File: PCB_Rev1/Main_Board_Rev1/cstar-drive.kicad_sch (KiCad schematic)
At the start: 0 parts

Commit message: LDO component files imported
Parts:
- added C15: C_Polarized, symbol Device:C_Polarized
- added CR1, CR2: SP4022-01FTG-C, CSTAR-MainBoard-Footprints:ZDO_SP4022_LTF, symbol SP4022_01FTG_C:SP4022-01FTG-C
- added D2, D3, D4, D5, D6, D7, D8, D9: D, symbol Device:D
- added J10, J9: B4B-PH-K-S, CSTAR-MainBoard-Footprints:B4B_PH_K_S, symbol B4B_PH_K_S:B4B-PH-K-S
- added U2: L298N, Package_TO_SOT_THT:TO-220-15_P2.54x2.54mm_StaggerOdd_Lead4.58mm_Vertical, symbol Driver_Motor:L298N
- added X1, X2: B2P-VH, CSTAR-MainBoard-Footprints:B2P-VH, symbol B2P-VH:B2P-VH
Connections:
- new net +3V3: J10.1, J9.1
- new net +5V: C15.1, D2.1 (K), D4.1 (K), D6.1 (K), D8.1 (K), U2.4 (Vs), U2.9 (Vss)
- new net Ch.A_MOTOR_1: J9.3
- new net Ch.A_MOTOR_2: J10.3
- new net Ch.B_MOTOR_1: J9.4
- new net Ch.B_MOTOR_2: J10.4
- new net EN_MOTOR_1: U2.6 (EnA)
- new net EN_MOTOR_2: U2.11 (EnB)
- new net GND: C15.2, D3.2 (A), D5.2 (A), D7.2 (A), D9.2 (A), J10.2, J9.2, U2.1 (SENSE_A), U2.15 (SENSE_B), U2.8 (GND)
- new net IN1_MOTOR_1: U2.5 (IN1)
- new net IN1_MOTOR_2: U2.10 (IN3)
- new net IN2_MOTOR_1: U2.7 (IN2)
- new net IN2_MOTOR_2: U2.12 (IN4)
- new net OUT1_MOTOR_1: CR1.2, D2.2 (A), D3.1 (K), U2.2 (OUT1), X1.1
- new net OUT1_MOTOR_2: CR2.2, D6.2 (A), D7.1 (K), U2.13 (OUT3), X2.1
- new net OUT2_MOTOR_1: CR1.1, D4.2 (A), D5.1 (K), U2.3 (OUT2), X1.2
- new net OUT2_MOTOR_2: CR2.1, D8.2 (A), D9.1 (K), U2.14 (OUT4), X2.2
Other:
- note added: "ENCODER 1 CONNECTION"
- note added: "ENCODER 2 CONNECTION"
- note added: "MOTOR 1 CONNECTION"
- note added: "MOTOR 2 CONNECTION"
- note added: "MOTOR DRIVE TRAIN SCHEMATIC"
- note added: "MOTOR DRIVER"

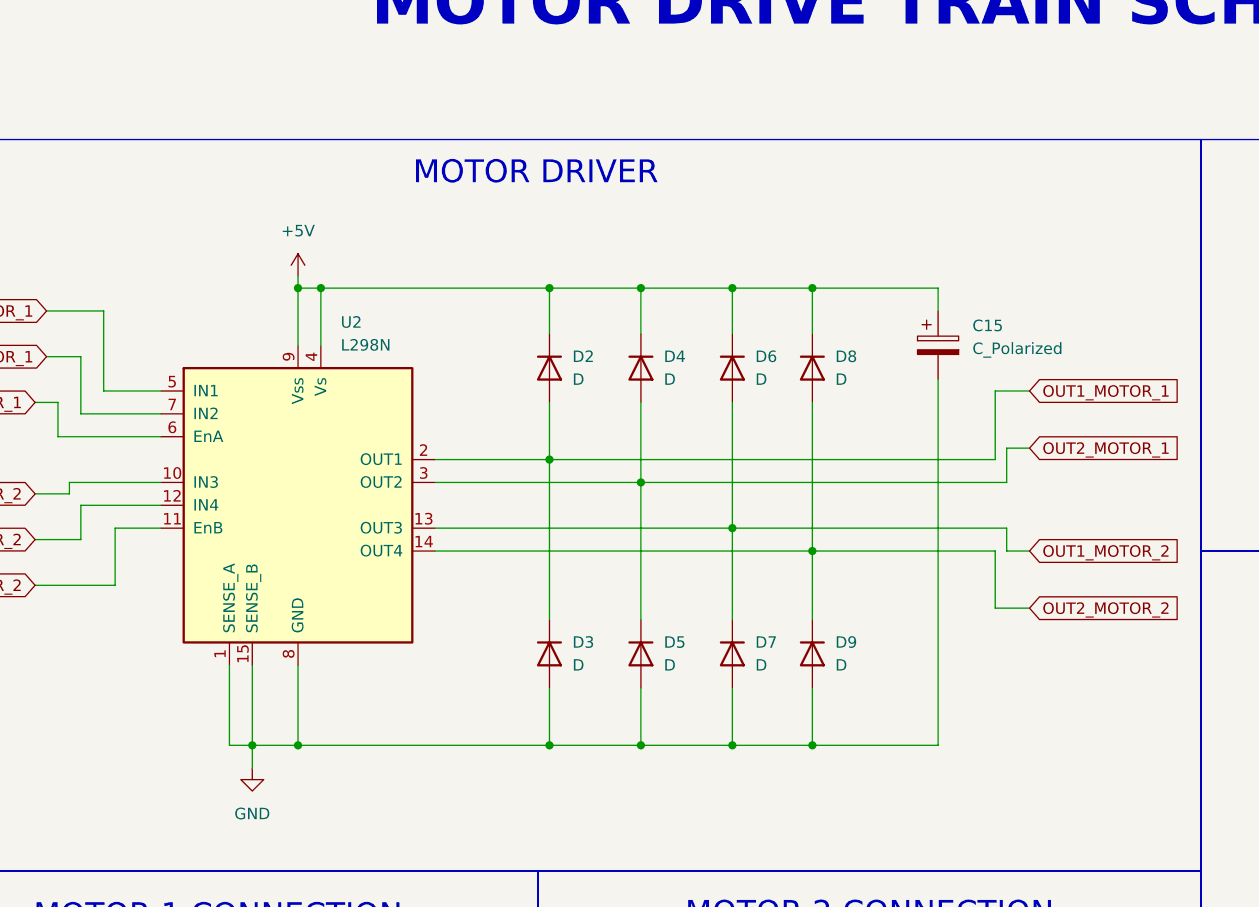
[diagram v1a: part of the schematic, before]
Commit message: Driver Schematic Update
Vss / Vs and decoupling capacitor updates
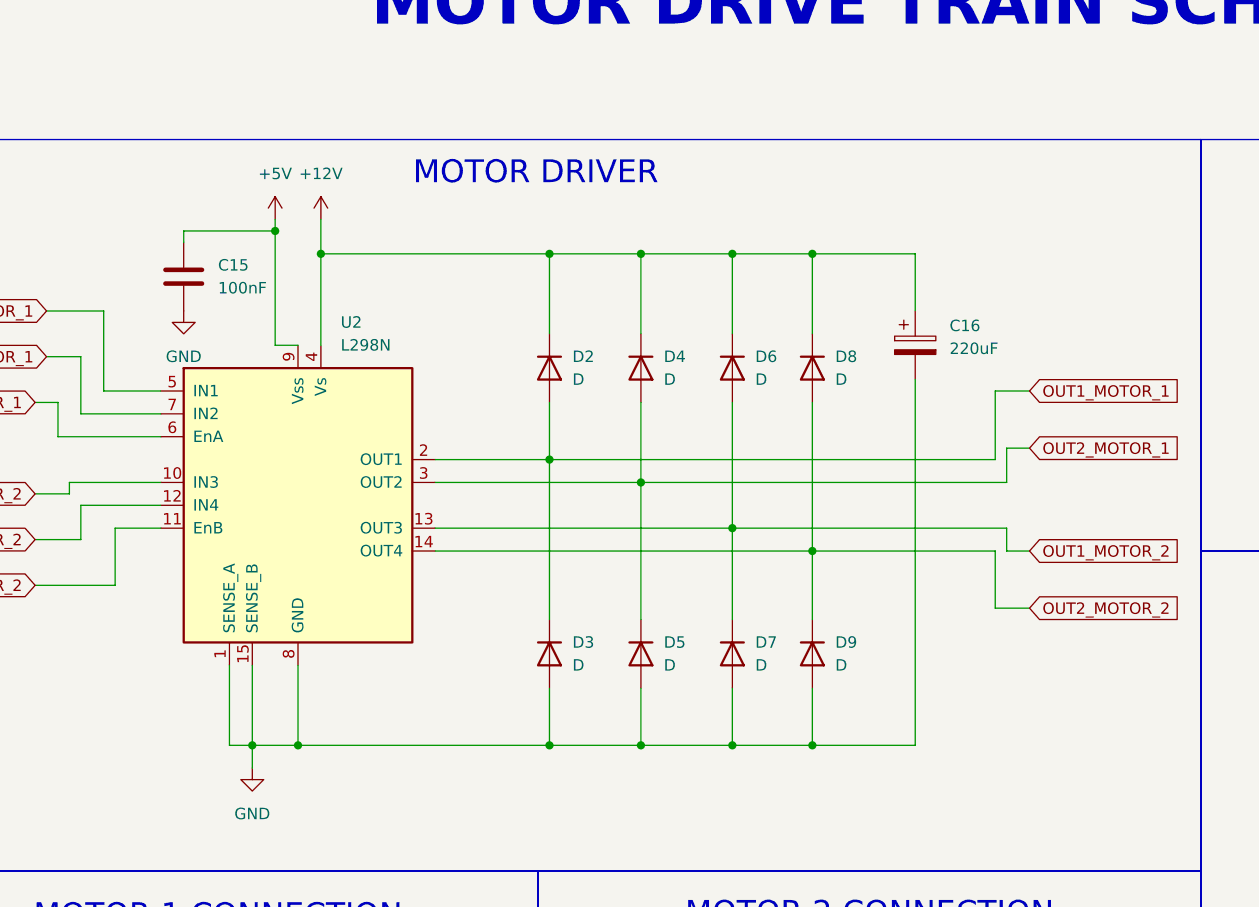
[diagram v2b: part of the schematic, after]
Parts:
- removed C15: C_Polarized, symbol Device:C_Polarized
- added C15: 100nF, symbol Device:C
- added C16: 220uF, symbol Device:C_Polarized
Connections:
- net +5V: now also C15.1; no longer D2.1 (K), D4.1 (K), D6.1 (K), D8.1 (K), U2.4 (Vs)
- net GND: now also C15.2, C16.2
- new net +12V: C16.1, D2.1 (K), D4.1 (K), D6.1 (K), D8.1 (K), U2.4 (Vs)

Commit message: Passives footprints changed
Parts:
- C15, C16: footprint (none) -> Capacitor_SMD:C_0805_2012Metric
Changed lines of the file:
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@@
 			)
 		)
-		(property "Footprint" ""
+		(property "Footprint" "Capacitor_SMD:C_0805_2012Metric"
 			(at 60.6552 62.23 0)
 			(effects
@@
 			)
 		)
-		(property "Footprint" ""
+		(property "Footprint" "Capacitor_SMD:C_0805_2012Metric"
 			(at 141.9352 69.85 0)
 			(effects

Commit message: Added new footprints
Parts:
- J10, J9: footprint CSTAR-MainBoard-Footprints:B4B_PH_K_S -> (none)
- X1, X2: footprint CSTAR-MainBoard-Footprints:B2P-VH -> (none)
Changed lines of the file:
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@@
 			)
 		)
-		(property "Footprint" "CSTAR-MainBoard-Footprints:B2P-VH"
+		(property "Footprint" ""
 			(at 41.91 149.86 0)
 			(effects
@@
 			)
 		)
-		(property "Footprint" "CSTAR-MainBoard-Footprints:B2P-VH"
+		(property "Footprint" ""
 			(at 113.03 149.86 0)
 			(effects
@@
 			)
 		)
-		(property "Footprint" "CSTAR-MainBoard-Footprints:B4B_PH_K_S"
+		(property "Footprint" ""
 			(at 195.58 74.93 0)
 			(effects
@@
 			)
 		)
-		(property "Footprint" "CSTAR-MainBoard-Footprints:B4B_PH_K_S"
+		(property "Footprint" ""
 			(at 199.39 120.65 0)
 			(effects

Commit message: more footprints changes
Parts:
- J10, J9: footprint (none) -> Footprints:B4B_PH_K_S
- X1, X2: footprint (none) -> Footprints:B2P-VH
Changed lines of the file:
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@@
 			)
 		)
-		(property "Footprint" ""
+		(property "Footprint" "Footprints:B2P-VH"
 			(at 41.91 149.86 0)
 			(effects
@@
 			)
 		)
-		(property "Footprint" ""
+		(property "Footprint" "Footprints:B2P-VH"
 			(at 113.03 149.86 0)
 			(effects
@@
 			)
 		)
-		(property "Footprint" ""
+		(property "Footprint" "Footprints:B4B_PH_K_S"
 			(at 195.58 74.93 0)
 			(effects
@@
 			)
 		)
-		(property "Footprint" ""
+		(property "Footprint" "Footprints:B4B_PH_K_S"
 			(at 199.39 120.65 0)
 			(effects

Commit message: diodes footprints added
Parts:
- D2, D3, D4, D5, D6, D7, D8, D9: footprint (none) -> Footprints:Diode_1N4007
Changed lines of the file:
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@@
 			)
 		)
-		(property "Footprint" ""
+		(property "Footprint" "Footprints:Diode_1N4007"
 			(at 129.54 68.58 0)
 			(effects
@@
 			)
 		)
-		(property "Footprint" ""
+		(property "Footprint" "Footprints:Diode_1N4007"
 			(at 110.49 100.33 0)
 			(effects
@@
 			)
 		)
-		(property "Footprint" ""
+		(property "Footprint" "Footprints:Diode_1N4007"
 			(at 110.49 68.58 0)
 			(effects
@@
 			)
 		)
-		(property "Footprint" ""
+		(property "Footprint" "Footprints:Diode_1N4007"
 			(at 129.54 100.33 0)
 			(effects
@@
 			)
 		)
-		(property "Footprint" ""
+		(property "Footprint" "Footprints:Diode_1N4007"
 			(at 100.33 68.58 0)
 			(effects
@@
 			)
 		)
-		(property "Footprint" ""
+		(property "Footprint" "Footprints:Diode_1N4007"
 			(at 100.33 100.33 0)
 			(effects
@@
 			)
 		)
-		(property "Footprint" ""
+		(property "Footprint" "Footprints:Diode_1N4007"
 			(at 120.65 68.58 0)
 			(effects
@@
 			)
 		)
-		(property "Footprint" ""
+		(property "Footprint" "Footprints:Diode_1N4007"
 			(at 120.65 100.33 0)
 			(effects

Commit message: more footprints assigned
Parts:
- CR1, CR2: footprint CSTAR-MainBoard-Footprints:ZDO_SP4022_LTF -> Footprints:TVSDiode
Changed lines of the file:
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@@
 			)
 		)
-		(property "Footprint" "CSTAR-MainBoard-Footprints:ZDO_SP4022_LTF"
+		(property "Footprint" "Footprints:TVSDiode"
 			(at 63.5 139.7 0)
 			(effects
@@
 			)
 		)
-		(property "Footprint" "CSTAR-MainBoard-Footprints:ZDO_SP4022_LTF"
+		(property "Footprint" "Footprints:TVSDiode"
 			(at 134.62 139.7 0)
 			(effects

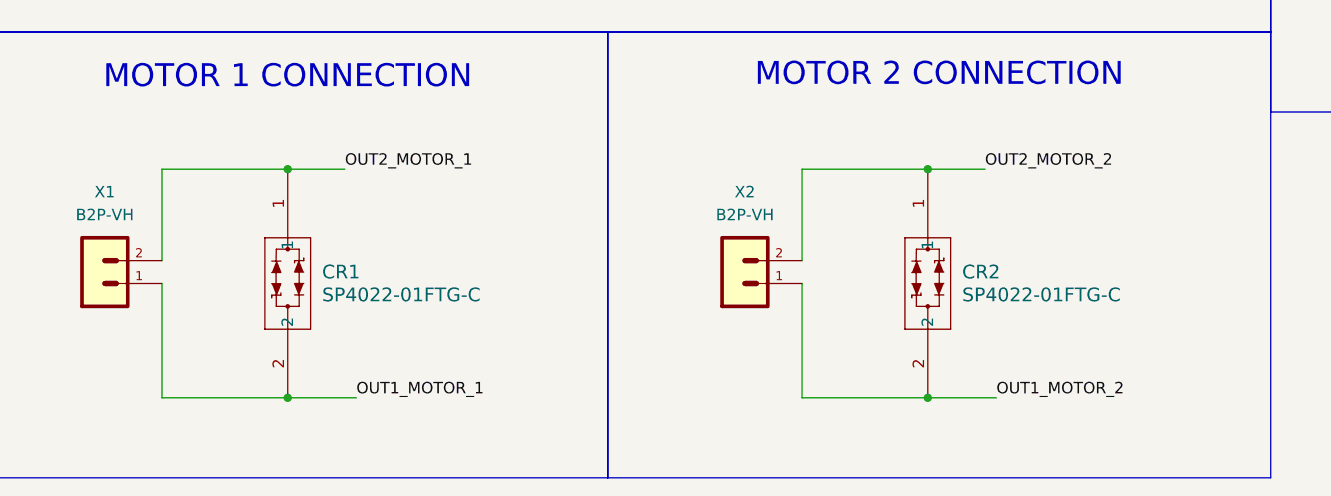
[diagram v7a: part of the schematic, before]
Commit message: Motor Drive Adjustment and Added Footprint for Polarized Cap
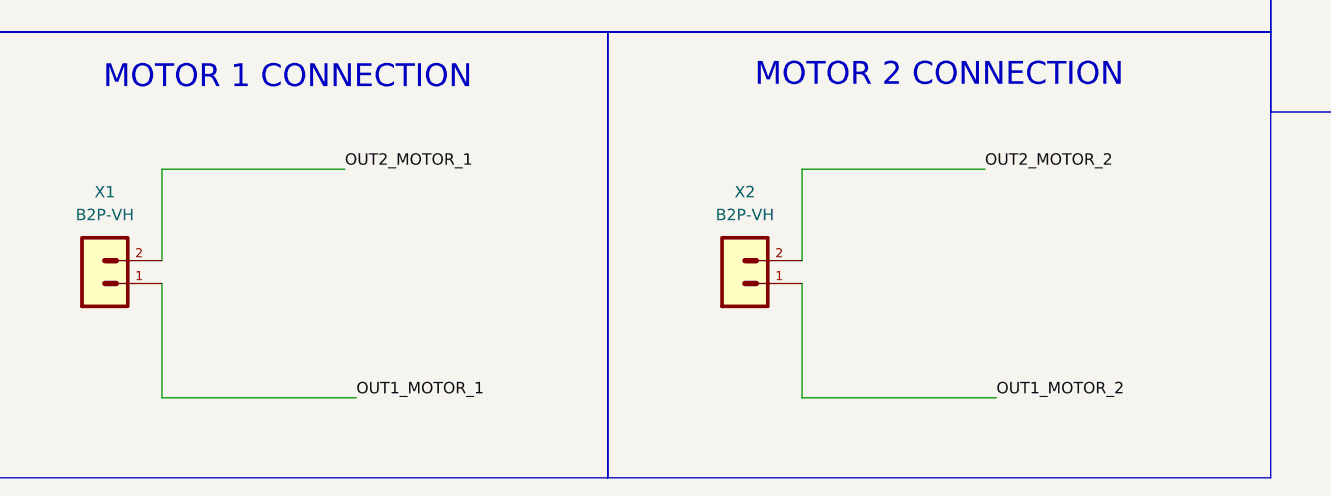
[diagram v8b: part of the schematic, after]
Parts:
- removed CR1, CR2: SP4022-01FTG-C, Footprints:TVSDiode, symbol SP4022_01FTG_C:SP4022-01FTG-C
- C16: footprint Capacitor_SMD:C_0805_2012Metric -> Footprints:Cap_Polarized_220uF
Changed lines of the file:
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@@
 	)
 	(junction
-		(at 63.5 139.7)
-		(diameter 0)
-		(color 0 0 0 0)
-	)
-	(junction
 		(at 129.54 55.88)
 		(diameter 0)
@@
 	)
 	(junction
-		(at 63.5 165.1)
-		(diameter 0)
-		(color 0 0 0 0)
-	)
-	(junction
 		(at 120.65 86.36)
 		(diameter 0)
@@
 	)
 	(junction
-		(at 134.62 165.1)
-		(diameter 0)
-		(color 0 0 0 0)
-	)
-	(junction
 		(at 120.65 55.88)
 		(diameter 0)
@@
 		(color 0 0 0 0)
 	)
-	(junction
-		(at 134.62 139.7)
-		(diameter 0)
-		(color 0 0 0 0)
-	)
 	(wire
 		(pts
@@
 	(wire
 		(pts
-			(xy 63.5 139.7) (xy 69.85 139.7)
+			(xy 49.53 139.7) (xy 69.85 139.7)
 		)
 		(stroke
@@
 	(wire
 		(pts
-			(xy 49.53 139.7) (xy 63.5 139.7)
-		)
-		(stroke
-			(width 0)
-			(type default)
-		)
-	)
-	(wire
-		(pts
 			(xy 100.33 55.88) (xy 110.49 55.88)
 		)
@@
 	(wire
 		(pts
-			(xy 49.53 165.1) (xy 63.5 165.1)
+			(xy 49.53 165.1) (xy 71.12 165.1)
 		)
 		(stroke
@@
 	(wire
 		(pts
-			(xy 134.62 139.7) (xy 140.97 139.7)
-		)
-		(stroke
-			(width 0)
-			(type default)
-		)
-	)
-	(wire
-		(pts
 			(xy 64.77 101.6) (xy 64.77 110.49)
 		)
@@
 	(wire
 		(pts
-			(xy 63.5 165.1) (xy 71.12 165.1)
-		)
-		(stroke
-			(width 0)
-			(type default)
-		)
-	)
-	(wire
-		(pts
 			(xy 140.97 69.85) (xy 140.97 110.49)
 		)
@@
 	(wire
 		(pts
-			(xy 120.65 165.1) (xy 134.62 165.1)
-		)
-		(stroke
-			(width 0)
-			(type default)
-		)
-	)
-	(wire
-		(pts
 			(xy 69.85 53.34) (xy 69.85 66.04)
 		)
@@
 	(wire
 		(pts
-			(xy 120.65 139.7) (xy 134.62 139.7)
+			(xy 120.65 139.7) (xy 140.97 139.7)
 		)
 		(stroke
@@
 	(wire
 		(pts
-			(xy 134.62 165.1) (xy 142.24 165.1)
+			(xy 120.65 165.1) (xy 142.24 165.1)
 		)
 		(stroke
@@
 	)
 	(symbol
-		(lib_id "SP4022_01FTG_C:SP4022-01FTG-C")
-		(at 63.5 139.7 270)
-		(unit 1)
-		(exclude_from_sim no)
-		(in_bom yes)
-		(on_board yes)
-		(dnp no)
-		(fields_autoplaced yes)
-		(property "Reference" "CR1"
-			(at 67.31 151.13 90)
-			(effects
-				(font
-					(size 1.524 1.524)
-				)
-				(justify left)
-			)
-		)
-		(property "Value" "SP4022-01FTG-C"
-			(at 67.31 153.67 90)
-			(effects
-				(font
-					(size 1.524 1.524)
-				)
-				(justify left)
-			)
-		)
-		(property "Footprint" "Footprints:TVSDiode"
-			(at 63.5 139.7 0)
-			(effects
-				(font
-					(size 1.27 1.27)
-					(italic yes)
-				)
-				(hide yes)
-			)
-		)
-		(property "Datasheet" "SP4022-01FTG-C"
-			(at 63.5 139.7 0)
-			(effects
-				(font
-					(size 1.27 1.27)
-					(italic yes)
-				)
-				(hide yes)
-			)
-		)
-		(property "Description" ""
-			(at 63.5 139.7 0)
-			(effects
-				(font
-					(size 1.27 1.27)
-				)
-				(hide yes)
-			)
-		)
-		(pin "1"
-		)
-		(pin "2"
-		)
-		(instances
-			(project "Main_Board_Rev1"
-				(path "/8f5a23de-a1fa-4202-92fb-c2ac3de0338c/0ea4e72d-54a3-4446-a173-a8fc45c421fe"
-					(reference "CR1")
-					(unit 1)
-				)
-			)
-		)
-	)
-	(symbol
 		(lib_id "Driver_Motor:L298N")
 		(at 72.39 83.82 0)
@@
 			)
 		)
-		(property "Footprint" "Capacitor_SMD:C_0805_2012Metric"
+		(property "Footprint" "Footprints:Cap_Polarized_220uF"
 			(at 141.9352 69.85 0)
 			(effects
@@
 					(unit 1)
 				)
-			)
-		)
-	)
-	(symbol
-		(lib_id "SP4022_01FTG_C:SP4022-01FTG-C")
-		(at 134.62 139.7 270)
-		(unit 1)
-		(exclude_from_sim no)
-		(in_bom yes)
-		(on_board yes)
-		(dnp no)
-		(fields_autoplaced yes)
-		(property "Reference" "CR2"
-			(at 138.43 151.13 90)
-			(effects
-				(font
-					(size 1.524 1.524)
-				)
-				(justify left)
-			)
-		)
-		(property "Value" "SP4022-01FTG-C"
-			(at 138.43 153.67 90)
-			(effects
-				(font
-					(size 1.524 1.524)
-				)
-				(justify left)
-			)
-		)
-		(property "Footprint" "Footprints:TVSDiode"
-			(at 134.62 139.7 0)
-			(effects
-				(font
-					(size 1.27 1.27)
-					(italic yes)
-				)
-				(hide yes)
-			)
-		)
-		(property "Datasheet" "SP4022-01FTG-C"
-			(at 134.62 139.7 0)
-			(effects
-				(font
-					(size 1.27 1.27)
-					(italic yes)
-				)
-				(hide yes)
-			)
-		)
-		(property "Description" ""
-			(at 134.62 139.7 0)
-			(effects
-				(font
-					(size 1.27 1.27)
-				)
-				(hide yes)
-			)
-		)
-		(pin "1"
-		)
-		(pin "2"
-		)
-		(instances
-			(project "Main_Board_Rev1"
-				(path "/8f5a23de-a1fa-4202-92fb-c2ac3de0338c/0ea4e72d-54a3-4446-a173-a8fc45c421fe"
-					(reference "CR2")
-					(unit 1)
-				)
